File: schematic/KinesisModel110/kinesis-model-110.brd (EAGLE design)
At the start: 100 x 80 mm, 25 parts, among them IC1 MEGA16-A, IC2 74LS138N, IC3 74LS138N, IC4 AT24CP, Q1 16mhz

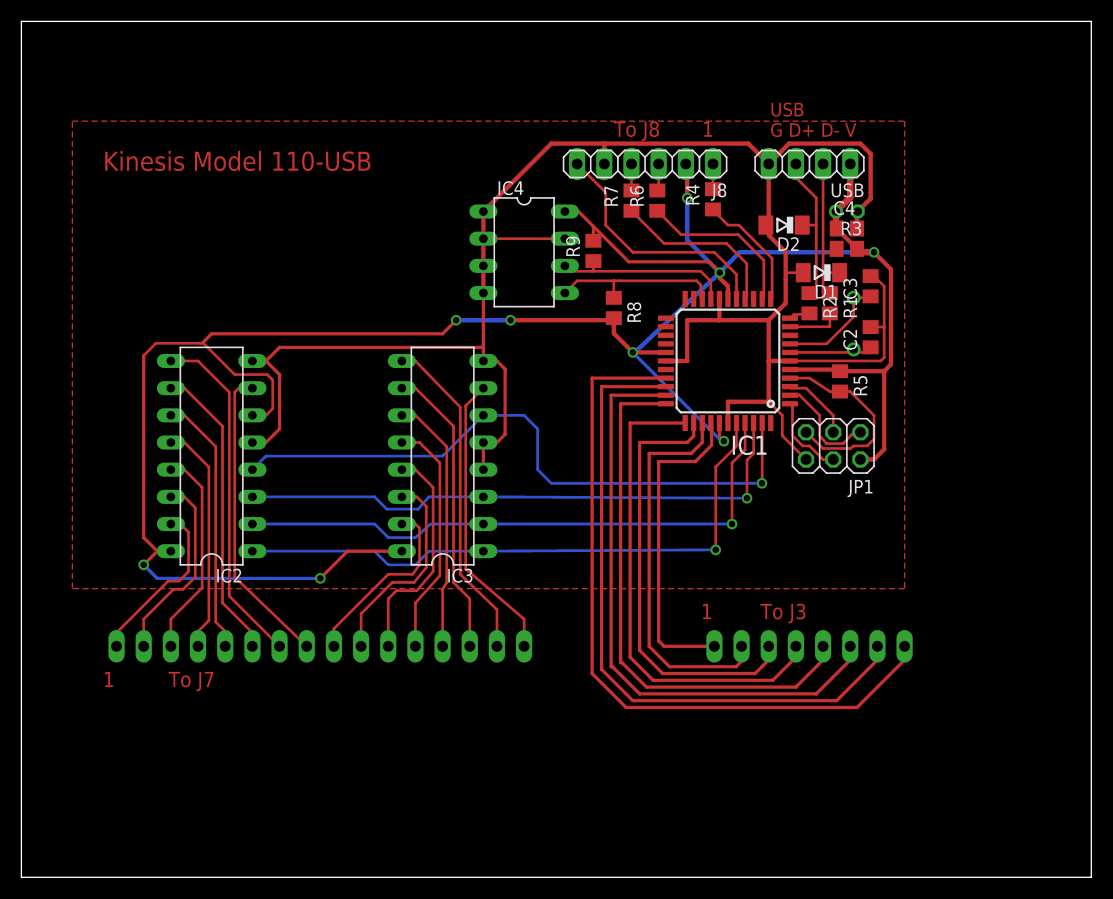
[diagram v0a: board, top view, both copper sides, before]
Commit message: Redesign Kinesis Model 110 PCB for 2-layer manufacturing
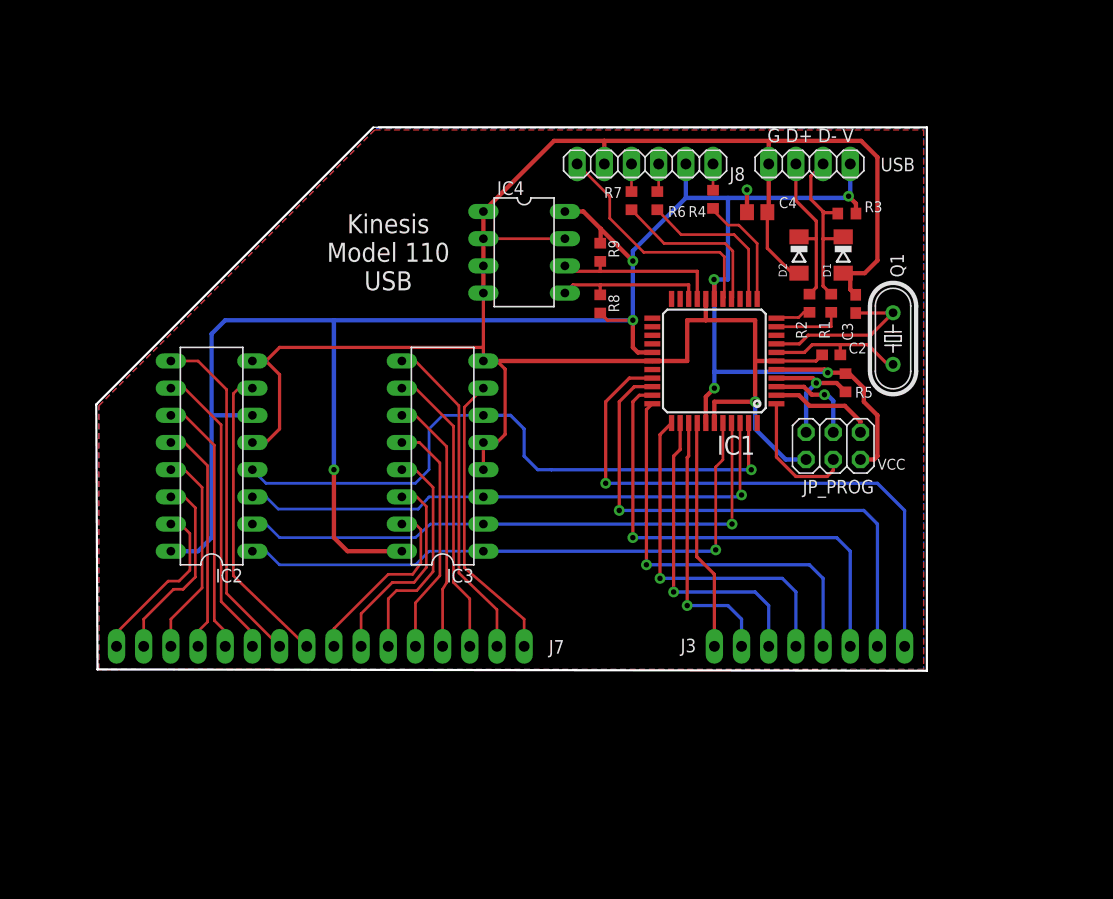
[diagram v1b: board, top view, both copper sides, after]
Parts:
- removed C1: 4u7, rcl:E2-5
- C2, C3: device rcl:C0805 -> rcl:C0603
- C4: value 100n -> 10uF
- R1, R2, R3, R4, R5, R6, R7, R8, R9: device rcl:R0805 -> rcl:R0603
- moved C4 8.52 mm to (68.8, 62.2)
- moved C2 4.04 mm to (75.7, 48.8), turned to 180 degrees
- moved Q1 3.94 mm to (81.5, 50.4), flipped to the top
- moved R3 3.30 mm to (77.2, 62.0)
- moved D2 3.12 mm to (72.7, 58.2), turned to 270 degrees
- moved D1 2.62 mm to (76.8, 58.2), turned to 270 degrees
- moved C3 2.16 mm to (78.0, 53.6)
- moved R8 1.33 mm to (54.1, 53.6)
- moved IC1 1.27 mm to (64.8, 48.3)
- moved R9 0.65 mm to (54.1, 58.4)
- moved R5 0.52 mm to (77.0, 46.2)
- moved R1 0.13 mm to (75.7, 53.7)
- renumbered JP1 to JP_PROG
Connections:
- net GND: no longer C1.-
- net VCC: no longer C1.+
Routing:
- net VCC: track 230.0 -> 204.3 mm, vias 9 -> 8
- net MATRIX8: track 68.1 -> 54.6 mm, vias 0 -> 1
- net MATRIX7: track 62.3 -> 49.9 mm, vias 0 -> 1
- net MATRIX4: track 45.3 -> 33.3 mm, vias 0 -> 1
- net MATRIX6: track 56.5 -> 44.5 mm, vias 0 -> 1
- net MATRIX5: track 50.6 -> 38.7 mm, vias 0 -> 1
- net MATRIX3: track 40.7 -> 29.3 mm, vias 0 -> 1
- net MATRIX2: track 36.3 -> 25.3 mm, vias 0 -> 1
- net MATRIX1: track 29.9 -> 21.6 mm
- net RST: track 18.7 -> 12.1 mm, vias 0 -> 1
- net GND: track 193.3 -> 199.5 mm, vias 0 -> 1
- net PIN10: track 10.4 -> 15.6 mm
- net PIN9: track 8.01 -> 12.9 mm
- net MOSI: track 7.89 -> 12.3 mm
- net EEP_SDA: track 16.3 -> 14.1 mm
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- added copper zone on layer 16, net GND
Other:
- board size 100 x 80 mm -> 77.6 x 50.8 mm
- board text added: "G D+ D- V"
- board text added: "Kinesis Model 110 USB"
- board text added: "VCC"
- board text removed: "1 To J3"
- board text removed: "1 To J7"
- board text removed: "Kinesis Model 110-USB"
- board text removed: "To J8 1"
- board text removed: "USB G D+ D- V"
